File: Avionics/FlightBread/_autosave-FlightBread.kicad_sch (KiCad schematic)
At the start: 24 parts, among them M1_POWER1 XING2/BL_HELI35A_POWER, M1_SIGNAL1 XING2/BL_HELI35A_SIGNAL, M2_POWER1 XING2/BL_HELI35A_POWER, M2_SIGNAL1 XING2/BL_HELI35A_SIGNAL

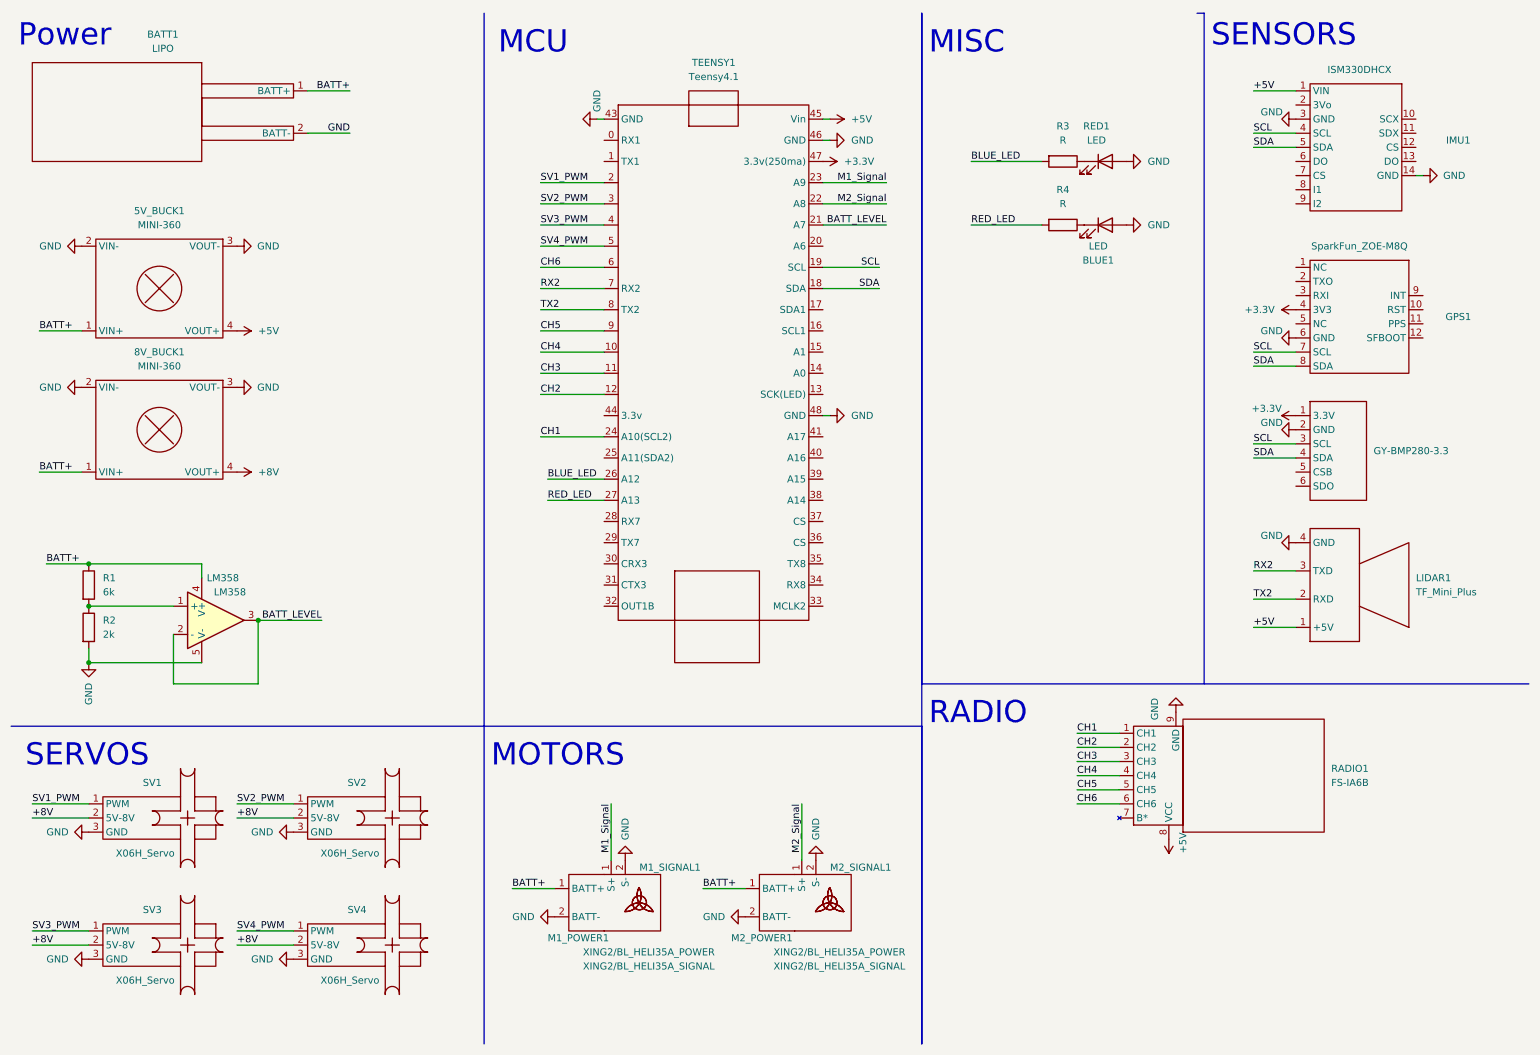
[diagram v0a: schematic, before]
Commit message: first board print, rushed but I wanna get somthing to start writing the code.....
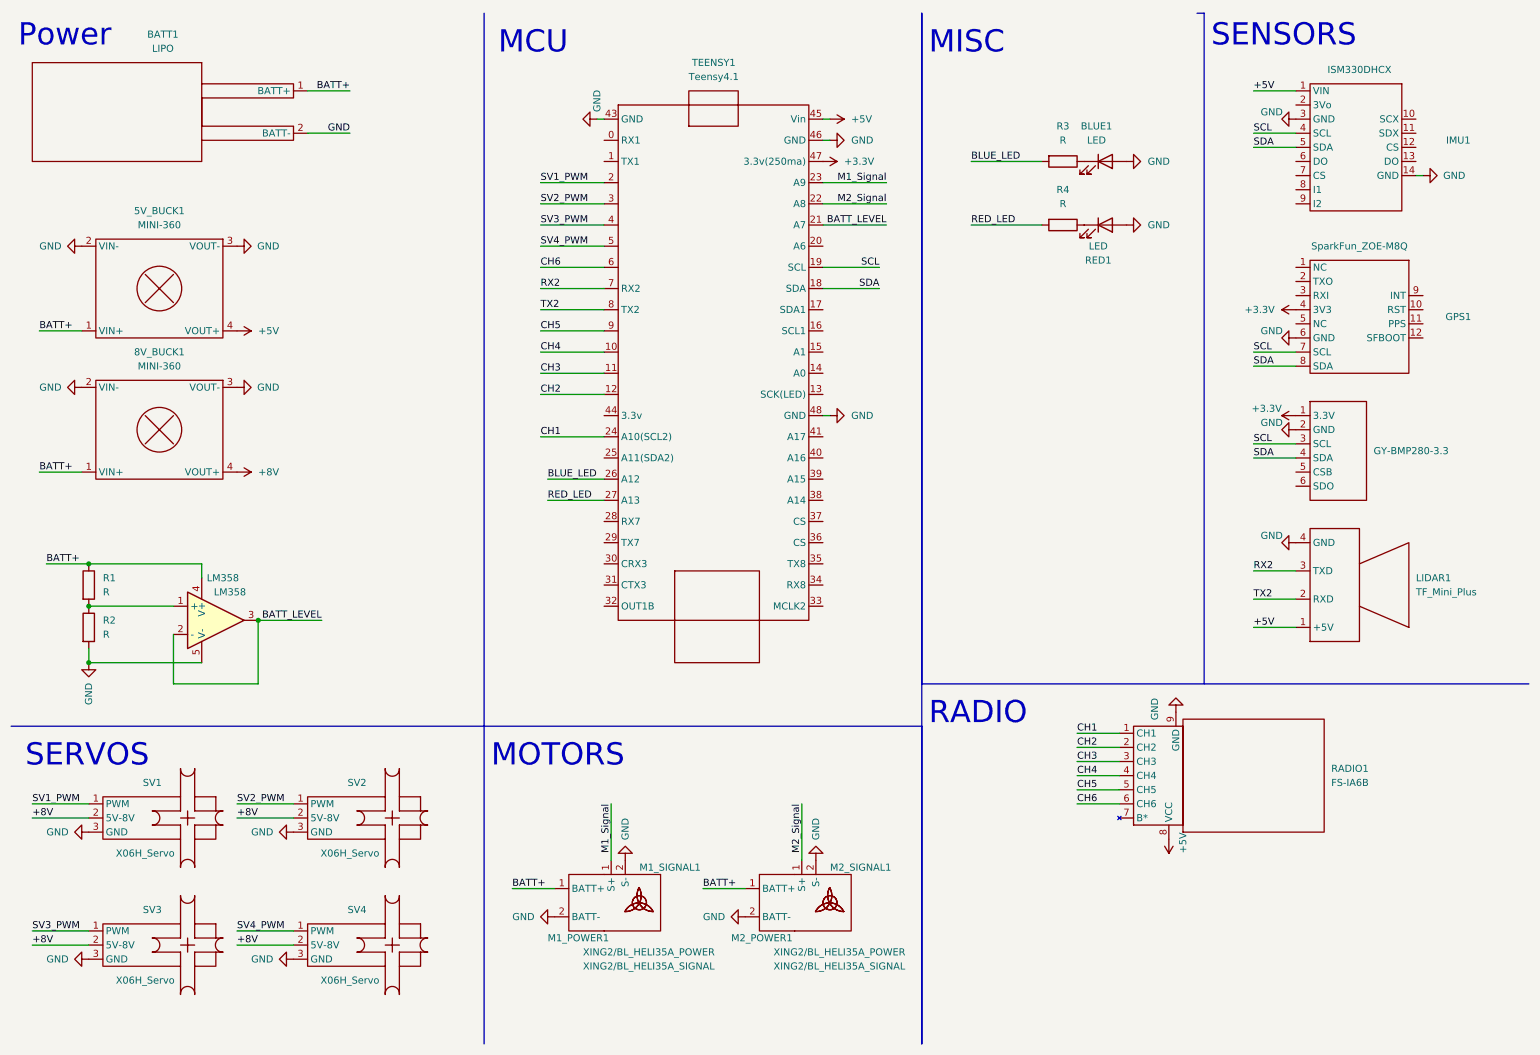
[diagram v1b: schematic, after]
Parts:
- R1: value 6k -> R
- R2: value 2k -> R
- renumbered RED1 to BLUE1, BLUE1 to RED1
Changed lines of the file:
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@@
       (effects (font (size 1.27 1.27)) (justify left))
     )
-    (property "Value" "2k" (id 1) (at 29.21 124.4599 0)
+    (property "Value" "R" (id 1) (at 29.21 124.4599 0)
       (effects (font (size 1.27 1.27)) (justify left))
     )
@@
   (symbol (lib_id "Device:LED") (at 209.55 50.8 0) (unit 1)
     (in_bom yes) (on_board yes)
-    (property "Reference" "BLUE1" (id 0) (at 208.28 57.15 0))
+    (property "Reference" "RED1" (id 0) (at 208.28 57.15 0))
     (property "Value" "LED" (id 1) (at 208.28 54.61 0))
     (property "Footprint" "UserKiCadFootprints:LED" (id 2) (at 209.55 50.8 0)
@@
       (effects (font (size 1.27 1.27)) (justify left))
     )
-    (property "Value" "6k" (id 1) (at 29.21 116.8399 0)
+    (property "Value" "R" (id 1) (at 29.21 116.8399 0)
       (effects (font (size 1.27 1.27)) (justify left))
     )
@@
   (symbol (lib_id "Device:LED") (at 209.55 39.37 0) (unit 1)
     (in_bom yes) (on_board yes) (fields_autoplaced)
-    (property "Reference" "RED1" (id 0) (at 207.9625 33.02 0))
+    (property "Reference" "BLUE1" (id 0) (at 207.9625 33.02 0))
     (property "Value" "LED" (id 1) (at 207.9625 35.56 0))
     (property "Footprint" "UserKiCadFootprints:LED" (id 2) (at 209.55 39.37 0)
@@
       (reference "BATT1") (unit 1) (value "LIPO") (footprint "UserKiCadFootprints:XT60_MOUNT")
     )
-    (path "/ee74ff6d-b41f-4c74-a993-13dd5c25e99b"
+    (path "/fe1c6224-af8a-4cd4-aba7-4fdcb9e56bf0"
       (reference "BLUE1") (unit 1) (value "LED") (footprint "UserKiCadFootprints:LED")
     )
@@
     )
     (path "/fcbbe054-232f-4e31-8d3b-fbffabeff3bc"
-      (reference "R1") (unit 1) (value "6k") (footprint "UserKiCadFootprints:pinhole_resistor")
+      (reference "R1") (unit 1) (value "R") (footprint "UserKiCadFootprints:pinhole_resistor")
     )
     (path "/1a4e8bc0-8d45-46fd-9ad4-5c97e9911464"
-      (reference "R2") (unit 1) (value "2k") (footprint "UserKiCadFootprints:pinhole_resistor")
+      (reference "R2") (unit 1) (value "R") (footprint "UserKiCadFootprints:pinhole_resistor")
     )
     (path "/bc316908-a33b-4bea-b56c-4d4678cbe951"
@@
       (reference "RADIO1") (unit 1) (value "FS-IA6B") (footprint "UserKiCadFootprints:FS-IA6B")
     )
-    (path "/fe1c6224-af8a-4cd4-aba7-4fdcb9e56bf0"
+    (path "/ee74ff6d-b41f-4c74-a993-13dd5c25e99b"
       (reference "RED1") (unit 1) (value "LED") (footprint "UserKiCadFootprints:LED")
     )
